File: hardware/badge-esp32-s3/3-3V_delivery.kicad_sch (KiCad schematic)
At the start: 5 parts, among them U2 NCP167BMX330TBG

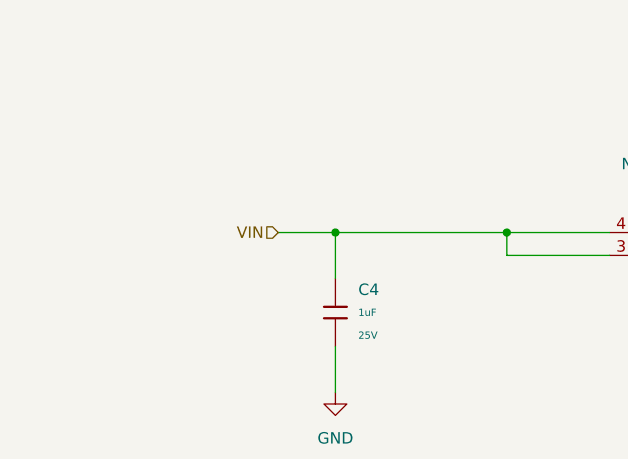
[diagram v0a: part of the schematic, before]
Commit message: Update 3-3V_delivery.kicad_sch
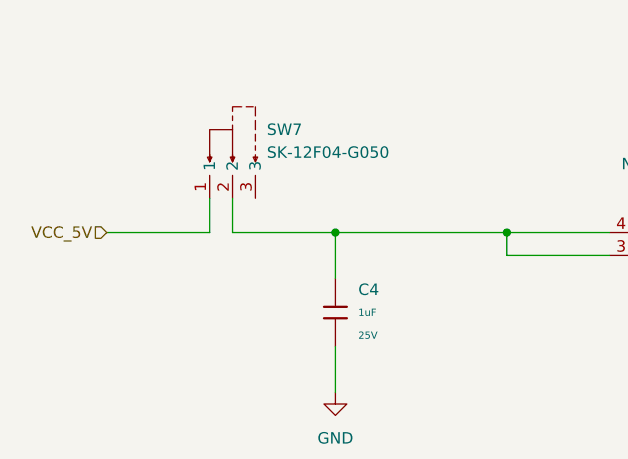
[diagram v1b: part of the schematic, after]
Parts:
- added SW7: SK-12F04-G050, lcsc-lib:SW-TH_G-SWITCH_SK-12F04-G050, symbol lcsc-lib:SK-12F04-G050
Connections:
- net VIN: no longer names the net of C4.1, U2.3 (EN), U2.4 (IN)
- net VIN: now also SW7.2
- new net VCC_5V: SW7.1
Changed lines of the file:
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@@
+	)
+	(junction
+		(at 107.95 63.5)
+		(diameter 0)
+		(color 0 0 0 0)
 	)
 	(junction
@@
 		(color 0 0 0 0)
 	)
-	(junction
-		(at 107.95 63.5)
-		(diameter 0)
-		(color 0 0 0 0)
-	)
 	(wire
 		(pts
@@
 	(wire
 		(pts
+			(xy 96.52 59.69) (xy 96.52 63.5)
+		)
+		(stroke
+			(width 0)
+			(type default)
+		)
+	)
+	(wire
+		(pts
 			(xy 151.13 77.47) (xy 146.05 77.47)
 		)
@@
 	(wire
 		(pts
+			(xy 82.55 63.5) (xy 93.98 63.5)
+		)
+		(stroke
+			(width 0)
+			(type default)
+		)
+	)
+	(wire
+		(pts
 			(xy 203.2 73.66) (xy 203.2 81.28)
 		)
@@
 	(wire
 		(pts
+			(xy 93.98 59.69) (xy 93.98 63.5)
+		)
+		(stroke
+			(width 0)
+			(type default)
+		)
+	)
+	(wire
+		(pts
 			(xy 151.13 73.66) (xy 151.13 77.47)
 		)
@@
 	(wire
 		(pts
-			(xy 101.6 63.5) (xy 107.95 63.5)
-		)
-		(stroke
-			(width 0)
-			(type default)
-		)
-	)
-	(wire
-		(pts
 			(xy 184.15 76.2) (xy 184.15 81.28)
 		)
@@
 		(pts
 			(xy 138.43 66.04) (xy 127 66.04)
+		)
+		(stroke
+			(width 0)
+			(type default)
+		)
+	)
+	(wire
+		(pts
+			(xy 96.52 63.5) (xy 107.95 63.5)
 		)
 		(stroke
@@
 		)
 	)
-	(hierarchical_label "VIN"
+	(hierarchical_label "VCC_5V"
 		(shape input)
-		(at 101.6 63.5 180)
+		(at 82.55 63.5 180)
 		(effects
 			(font
@@
 					(unit 1)
 				)
+			)
+		)
+	)
+	(symbol
+		(lib_id "lcsc-lib:SK-12F04-G050")
+		(at 96.52 54.61 0)
+		(unit 1)
+		(exclude_from_sim no)
+		(in_bom yes)
+		(on_board yes)
+		(dnp no)
+		(fields_autoplaced yes)
+		(property "Reference" "SW7"
+			(at 100.33 52.0699 0)
+			(effects
+				(font
+					(size 1.27 1.27)
+				)
+				(justify left)
+			)
+		)
+		(property "Value" "SK-12F04-G050"
+			(at 100.33 54.6099 0)
+			(effects
+				(font
+					(size 1.27 1.27)
+				)
+				(justify left)
+			)
+		)
+		(property "Footprint" "lcsc-lib:SW-TH_G-SWITCH_SK-12F04-G050"
+			(at 96.52 67.31 0)
+			(effects
+				(font
+					(size 1.27 1.27)
+				)
+				(hide yes)
+			)
+		)
+		(property "Datasheet" ""
+			(at 96.52 54.61 0)
+			(effects
+				(font
+					(size 1.27 1.27)
+				)
+				(hide yes)
+			)
+		)
+		(property "Description" ""
+			(at 96.52 54.61 0)
+			(effects
+				(font
+					(size 1.27 1.27)
+				)
+				(hide yes)
+			)
+		)
+		(property "LCSC Part" "C2848876"
+			(at 96.52 69.85 0)
+			(effects
+				(font
+					(size 1.27 1.27)
+				)
+				(hide yes)
+			)
+		)
+		(pin "2"
+		)
+		(pin "1"
+		)
+		(pin "3"
+		)
+		(instances
+			(project ""
+				(path "/e2af9a6c-dbe9-4de2-9ba6-ea213a7300ec/f36e3e2c-eb39-474f-a489-171fecc16703"
+					(reference "SW7")
+					(unit 1)
+				)

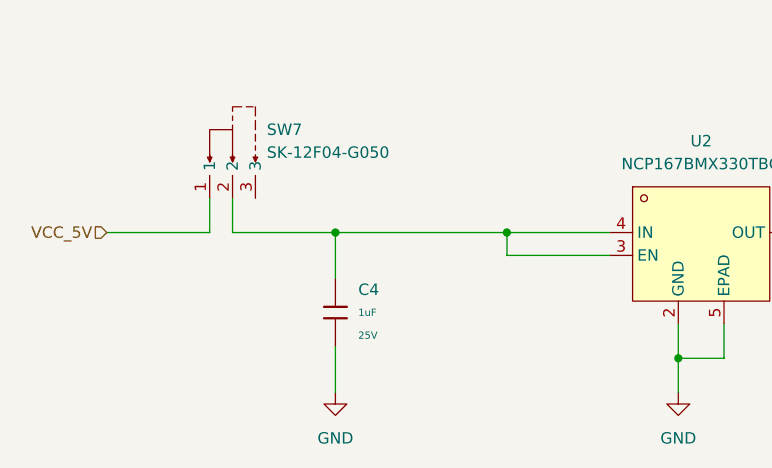
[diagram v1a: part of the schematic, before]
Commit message: Switch on LDO enable pin
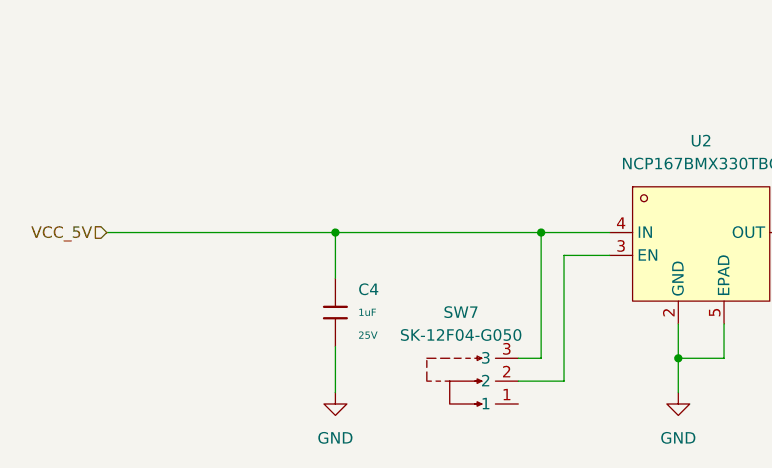
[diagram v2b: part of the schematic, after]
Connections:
- net VCC_5V: now also C4.1, SW7.3, U2.4 (IN); no longer SW7.1
- net at SW7.2, U2.3 (EN): no longer C4.1, U2.4 (IN)
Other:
- moved on the sheet: SW7
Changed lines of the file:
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@@
-	)
-	(junction
-		(at 127 63.5)
-		(diameter 0)
-		(color 0 0 0 0)
 	)
 	(junction
@@
 		(color 0 0 0 0)
 	)
+	(junction
+		(at 130.81 63.5)
+		(diameter 0)
+		(color 0 0 0 0)
+	)
 	(wire
 		(pts
@@
 	(wire
 		(pts
-			(xy 96.52 59.69) (xy 96.52 63.5)
-		)
-		(stroke
-			(width 0)
-			(type default)
-		)
-	)
-	(wire
-		(pts
 			(xy 151.13 77.47) (xy 146.05 77.47)
 		)
@@
 	(wire
 		(pts
-			(xy 127 66.04) (xy 127 63.5)
-		)
-		(stroke
-			(width 0)
-			(type default)
-		)
-	)
-	(wire
-		(pts
-			(xy 82.55 63.5) (xy 93.98 63.5)
+			(xy 82.55 63.5) (xy 107.95 63.5)
 		)
 		(stroke
@@
 	(wire
 		(pts
-			(xy 107.95 63.5) (xy 127 63.5)
+			(xy 128.27 80.01) (xy 133.35 80.01)
 		)
 		(stroke
@@
 	(wire
 		(pts
-			(xy 93.98 59.69) (xy 93.98 63.5)
-		)
-		(stroke
-			(width 0)
-			(type default)
-		)
-	)
-	(wire
-		(pts
 			(xy 151.13 73.66) (xy 151.13 77.47)
 		)
@@
 	(wire
 		(pts
+			(xy 130.81 77.47) (xy 130.81 63.5)
+		)
+		(stroke
+			(width 0)
+			(type default)
+		)
+	)
+	(wire
+		(pts
 			(xy 184.15 76.2) (xy 184.15 81.28)
 		)
@@
 	(wire
 		(pts
+			(xy 130.81 63.5) (xy 138.43 63.5)
+		)
+		(stroke
+			(width 0)
+			(type default)
+		)
+	)
+	(wire
+		(pts
 			(xy 200.66 63.5) (xy 203.2 63.5)
 		)
@@
 	(wire
 		(pts
-			(xy 127 63.5) (xy 138.43 63.5)
+			(xy 133.35 66.04) (xy 133.35 80.01)
+		)
+		(stroke
+			(width 0)
+			(type default)
+		)
+	)
+	(wire
+		(pts
+			(xy 107.95 63.5) (xy 130.81 63.5)
+		)
+		(stroke
+			(width 0)
+			(type default)
+		)
+	)
+	(wire
+		(pts
+			(xy 138.43 66.04) (xy 133.35 66.04)
 		)
 		(stroke
@@
 	(wire
 		(pts
-			(xy 138.43 66.04) (xy 127 66.04)
-		)
-		(stroke
-			(width 0)
-			(type default)
-		)
-	)
-	(wire
-		(pts
-			(xy 96.52 63.5) (xy 107.95 63.5)
+			(xy 128.27 77.47) (xy 130.81 77.47)
 		)
 		(stroke
@@
 	(symbol
 		(lib_id "lcsc-lib:SK-12F04-G050")
-		(at 96.52 54.61 0)
+		(at 123.19 80.01 90)
 		(unit 1)
 		(exclude_from_sim no)
@@
 		(fields_autoplaced yes)
 		(property "Reference" "SW7"
-			(at 100.33 52.0699 0)
-			(effects
-				(font
-					(size 1.27 1.27)
-				)
-				(justify left)
+			(at 121.92 72.39 90)
+			(effects
+				(font
+					(size 1.27 1.27)
+				)
 			)
 		)
 		(property "Value" "SK-12F04-G050"
-			(at 100.33 54.6099 0)
-			(effects
-				(font
-					(size 1.27 1.27)
-				)
-				(justify left)
+			(at 121.92 74.93 90)
+			(effects
+				(font
+					(size 1.27 1.27)
+				)
 			)
 		)
 		(property "Footprint" "lcsc-lib:SW-TH_G-SWITCH_SK-12F04-G050"
-			(at 96.52 67.31 0)
+			(at 135.89 80.01 0)
 			(effects
 				(font
@@
 		)
 		(property "Datasheet" ""
-			(at 96.52 54.61 0)
+			(at 123.19 80.01 0)
 			(effects
 				(font
@@
 		)
 		(property "Description" ""
-			(at 96.52 54.61 0)
+			(at 123.19 80.01 0)
 			(effects
 				(font
@@
 		)
 		(property "LCSC Part" "C2848876"
-			(at 96.52 69.85 0)
-			(effects
-				(font
+			(at 138.43 80.01 0)
+			(effects
+				(font

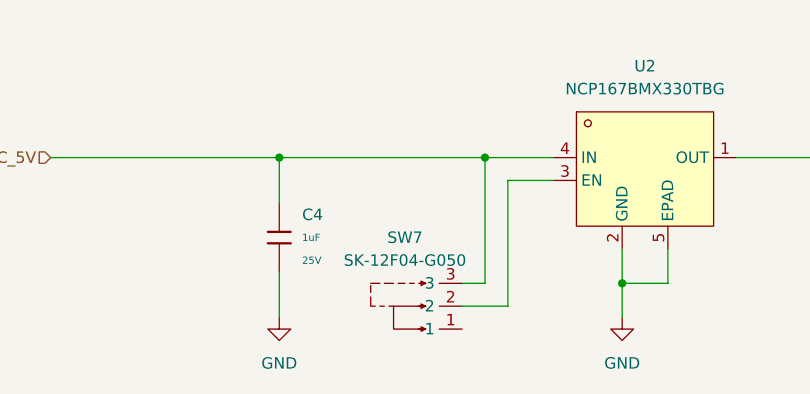
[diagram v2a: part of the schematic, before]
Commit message: Moved Switch posistion
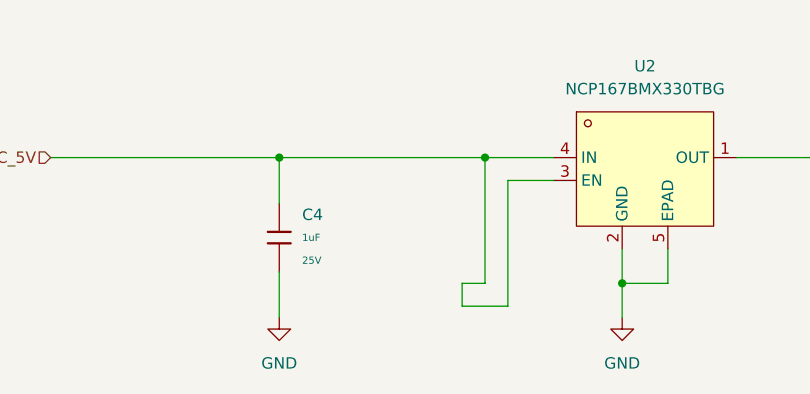
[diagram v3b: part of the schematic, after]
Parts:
- removed SW7: SK-12F04-G050, lcsc-lib:SW-TH_G-SWITCH_SK-12F04-G050, symbol lcsc-lib:SK-12F04-G050
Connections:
- net VCC_5V: now also U2.3 (EN)
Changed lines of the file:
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@@
+	(wire
+		(pts
+			(xy 128.27 77.47) (xy 128.27 80.01)
+		)
+		(stroke
+			(width 0)
+			(type default)
+		)
+	)
 	(wire
 		(pts
@@
 					(unit 1)
 				)
-			)
-		)
-	)
-	(symbol
-		(lib_id "lcsc-lib:SK-12F04-G050")
-		(at 123.19 80.01 90)
-		(unit 1)
-		(exclude_from_sim no)
-		(in_bom yes)
-		(on_board yes)
-		(dnp no)
-		(fields_autoplaced yes)
-		(property "Reference" "SW7"
-			(at 121.92 72.39 90)
-			(effects
-				(font
-					(size 1.27 1.27)
-				)
-			)
-		)
-		(property "Value" "SK-12F04-G050"
-			(at 121.92 74.93 90)
-			(effects
-				(font
-					(size 1.27 1.27)
-				)
-			)
-		)
-		(property "Footprint" "lcsc-lib:SW-TH_G-SWITCH_SK-12F04-G050"
-			(at 135.89 80.01 0)
-			(effects
-				(font
-					(size 1.27 1.27)
-				)
-				(hide yes)
-			)
-		)
-		(property "Datasheet" ""
-			(at 123.19 80.01 0)
-			(effects
-				(font
-					(size 1.27 1.27)
-				)
-				(hide yes)
-			)
-		)
-		(property "Description" ""
-			(at 123.19 80.01 0)
-			(effects
-				(font
-					(size 1.27 1.27)
-				)
-				(hide yes)
-			)
-		)
-		(property "LCSC Part" "C2848876"
-			(at 138.43 80.01 0)
-			(effects
-				(font
-					(size 1.27 1.27)
-				)
-				(hide yes)
-			)
-		)
-		(pin "2"
-		)
-		(pin "1"
-		)
-		(pin "3"
-		)
-		(instances
-			(project ""
-				(path "/e2af9a6c-dbe9-4de2-9ba6-ea213a7300ec/f36e3e2c-eb39-474f-a489-171fecc16703"
-					(reference "SW7")
-					(unit 1)
-				)

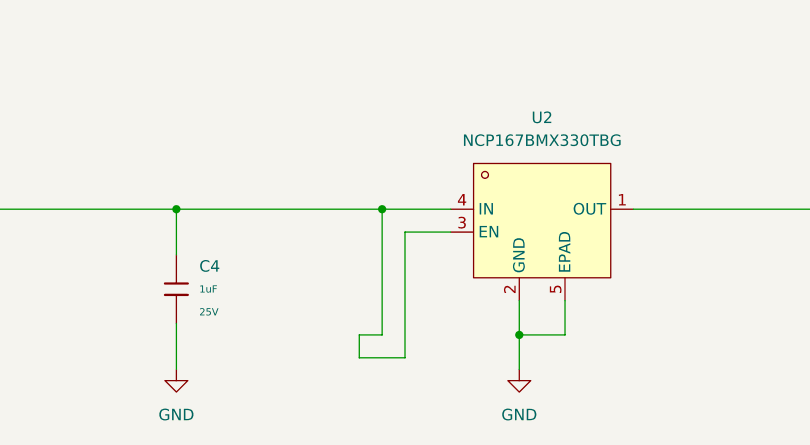
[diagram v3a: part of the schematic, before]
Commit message: Fleshed out schematic with all exposed pins
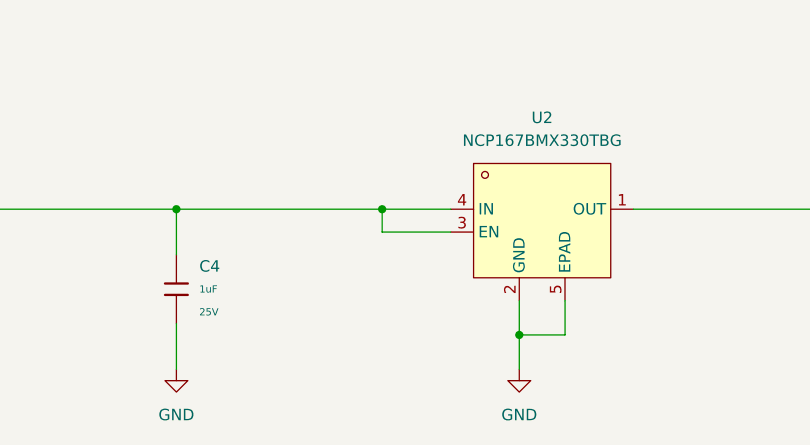
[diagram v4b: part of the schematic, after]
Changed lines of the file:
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@@
-	(wire
-		(pts
-			(xy 128.27 80.01) (xy 133.35 80.01)
-		)
-		(stroke
-			(width 0)
-			(type default)
-		)
-	)
 	(wire
 		(pts
@@
 	(wire
 		(pts
-			(xy 128.27 77.47) (xy 128.27 80.01)
-		)
-		(stroke
-			(width 0)
-			(type default)
-		)
-	)
-	(wire
-		(pts
 			(xy 158.75 63.5) (xy 184.15 63.5)
 		)
@@
 	(wire
 		(pts
-			(xy 130.81 77.47) (xy 130.81 63.5)
+			(xy 130.81 66.04) (xy 130.81 63.5)
 		)
 		(stroke
@@
 	(wire
 		(pts
-			(xy 133.35 66.04) (xy 133.35 80.01)
-		)
-		(stroke
-			(width 0)
-			(type default)
-		)
-	)
-	(wire
-		(pts
 			(xy 107.95 63.5) (xy 130.81 63.5)
-		)
-		(stroke
-			(width 0)
-			(type default)
-		)
-	)
-	(wire
-		(pts
-			(xy 138.43 66.04) (xy 133.35 66.04)
 		)
 		(stroke
@@
 	(wire
 		(pts
-			(xy 128.27 77.47) (xy 130.81 77.47)
+			(xy 130.81 66.04) (xy 138.43 66.04)
 		)
 		(stroke

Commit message: Annotate schematic
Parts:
- renumbered C4 to C3, C3 to C4, D9 to D1
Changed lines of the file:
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@@
 		(dnp no)
 		(fields_autoplaced yes)
-		(property "Reference" "#PWR018"
+		(property "Reference" "#PWR04"
 			(at 107.95 87.63 0)
 			(effects
@@
 			(project ""
 				(path "/e2af9a6c-dbe9-4de2-9ba6-ea213a7300ec/f36e3e2c-eb39-474f-a489-171fecc16703"
-					(reference "#PWR018")
+					(reference "#PWR04")
 					(unit 1)
 				)
@@
 		(dnp no)
 		(fields_autoplaced yes)
-		(property "Reference" "D9"
+		(property "Reference" "D1"
 			(at 205.74 68.4846 0)
 			(effects
@@
 			(project ""
 				(path "/e2af9a6c-dbe9-4de2-9ba6-ea213a7300ec/f36e3e2c-eb39-474f-a489-171fecc16703"
-					(reference "D9")
+					(reference "D1")
 					(unit 1)
 				)
@@
 		(dnp no)
 		(fields_autoplaced yes)
-		(property "Reference" "C3"
+		(property "Reference" "C4"
 			(at 186.69 69.8499 0)
 			(effects
@@
 			(project ""
 				(path "/e2af9a6c-dbe9-4de2-9ba6-ea213a7300ec/f36e3e2c-eb39-474f-a489-171fecc16703"
-					(reference "C3")
+					(reference "C4")
 					(unit 1)
 				)
@@
 		(dnp no)
 		(fields_autoplaced yes)
-		(property "Reference" "C4"
+		(property "Reference" "C3"
 			(at 110.49 69.8499 0)
 			(effects
@@
 			(project ""
 				(path "/e2af9a6c-dbe9-4de2-9ba6-ea213a7300ec/f36e3e2c-eb39-474f-a489-171fecc16703"
-					(reference "C4")
+					(reference "C3")
 					(unit 1)
 				)
@@
 		(dnp no)
 		(fields_autoplaced yes)
-		(property "Reference" "#PWR017"
+		(property "Reference" "#PWR05"
 			(at 146.05 87.63 0)
 			(effects
@@
 			(project ""
 				(path "/e2af9a6c-dbe9-4de2-9ba6-ea213a7300ec/f36e3e2c-eb39-474f-a489-171fecc16703"
-					(reference "#PWR017")
+					(reference "#PWR05")
 					(unit 1)
 				)
@@
 		(dnp no)
 		(fields_autoplaced yes)
-		(property "Reference" "#PWR019"
+		(property "Reference" "#PWR06"
 			(at 184.15 87.63 0)
 			(effects
@@
 			(project ""
 				(path "/e2af9a6c-dbe9-4de2-9ba6-ea213a7300ec/f36e3e2c-eb39-474f-a489-171fecc16703"
-					(reference "#PWR019")
+					(reference "#PWR06")
 					(unit 1)
 				)
@@
 		(dnp no)
 		(fields_autoplaced yes)
-		(property "Reference" "#PWR020"
+		(property "Reference" "#PWR07"
 			(at 203.2 87.63 0)
 			(effects
@@
 			(project ""
 				(path "/e2af9a6c-dbe9-4de2-9ba6-ea213a7300ec/f36e3e2c-eb39-474f-a489-171fecc16703"
-					(reference "#PWR020")
+					(reference "#PWR07")
 					(unit 1)
 				)
